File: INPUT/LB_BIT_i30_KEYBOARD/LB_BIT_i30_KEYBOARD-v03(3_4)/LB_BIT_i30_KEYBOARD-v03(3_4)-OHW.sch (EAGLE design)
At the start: 53 parts

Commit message: Updated licenses
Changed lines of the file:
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@@
 <?xml version="1.0" encoding="utf-8"?>
 <!DOCTYPE eagle SYSTEM "eagle.dtd">
-<eagle version="6.4">
+<eagle version="6.6.0">
 <drawing>
 <settings>
@@
 <layer number="225" name="225bmp" color="26" fill="10" visible="no" active="yes"/>
 <layer number="226" name="226bmp" color="27" fill="10" visible="no" active="yes"/>
+<layer number="227" name="227bmp" color="7" fill="1" visible="yes" active="yes"/>
+<layer number="228" name="228bmp" color="7" fill="1" visible="yes" active="yes"/>
 <layer number="248" name="Housing" color="7" fill="1" visible="yes" active="yes"/>
 <layer number="249" name="Edge" color="7" fill="1" visible="yes" active="yes"/>
@@
 <instance part="GND8" gate="1" x="43.18" y="5.08"/>
 <instance part="GND18" gate="1" x="187.96" y="78.74"/>
-<instance part="U$1" gate="G$1" x="236.22" y="50.8"/>
+<instance part="U$1" gate="G$1" x="20.32" y="12.7"/>
 <instance part="I30TVS3" gate="G$1" x="215.9" y="144.78" smashed="yes">
 <attribute name="NAME" x="212.8774" y="134.62" size="1.778" layer="95" rot="R90"/>
@@
 <instance part="GND19" gate="1" x="215.9" y="134.62"/>
 <instance part="GND20" gate="1" x="55.88" y="58.42"/>
-<instance part="U$2" gate="G$1" x="152.4" y="45.72"/>
+<instance part="U$2" gate="G$1" x="149.86" y="43.18"/>
 </instances>
 <busses>

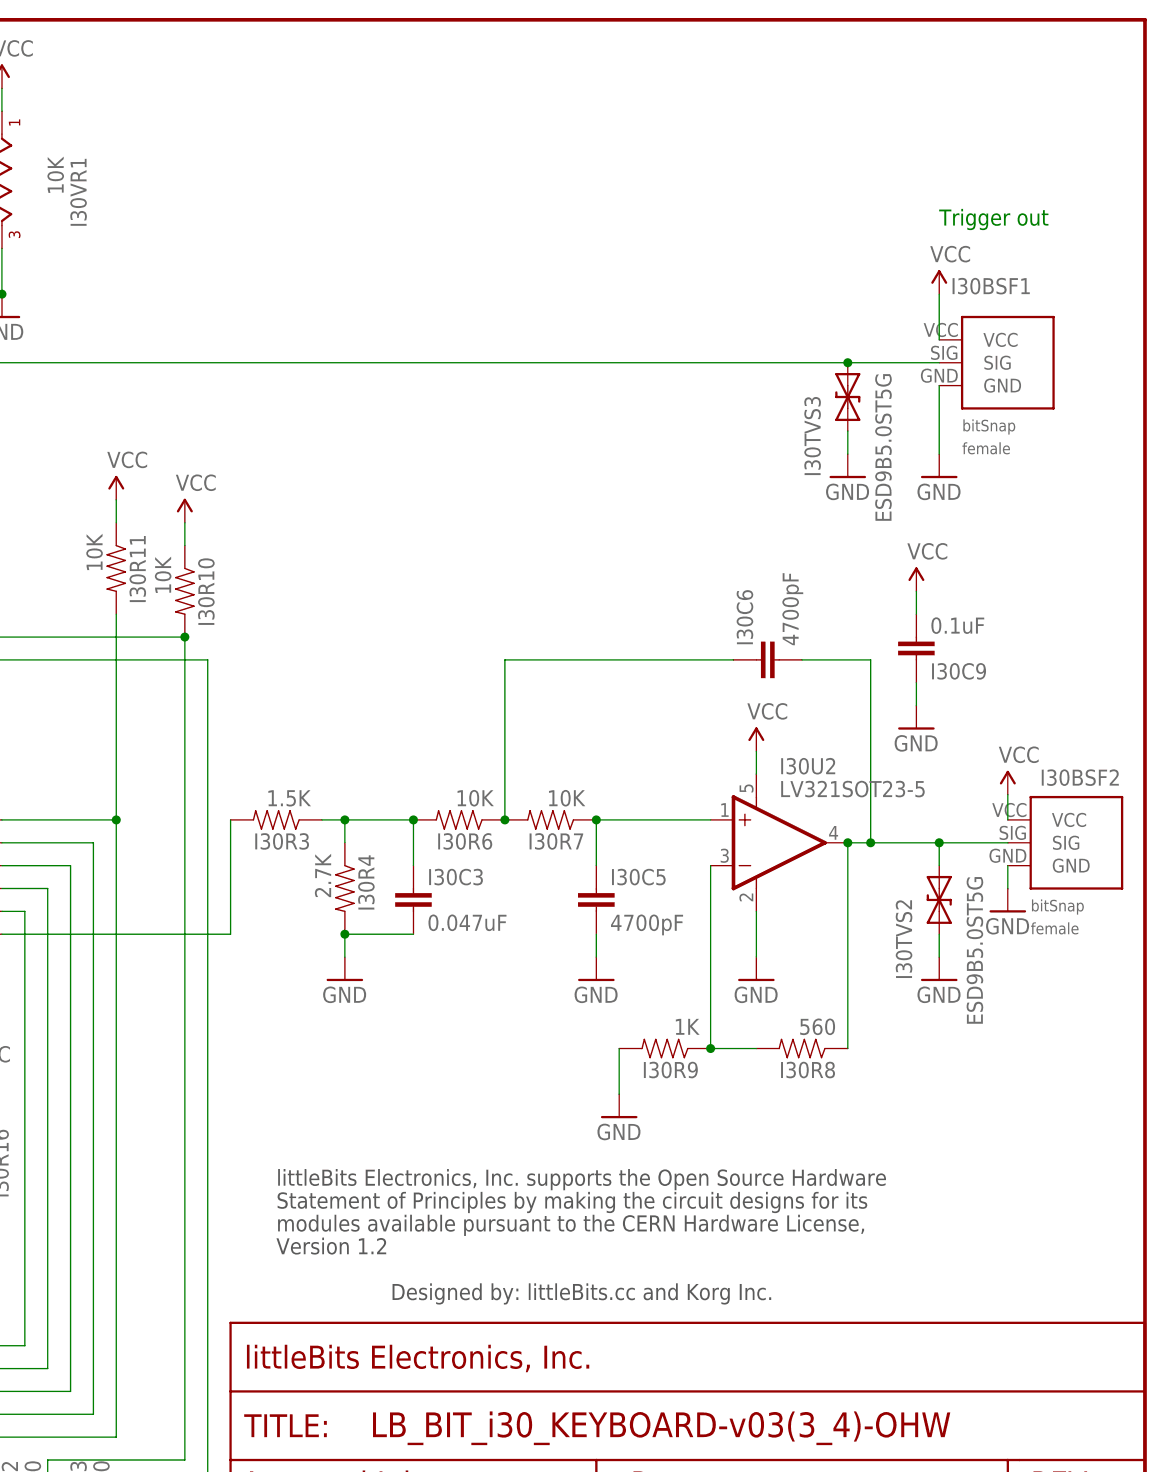
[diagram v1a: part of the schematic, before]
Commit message: Updated license in Korg bits modules
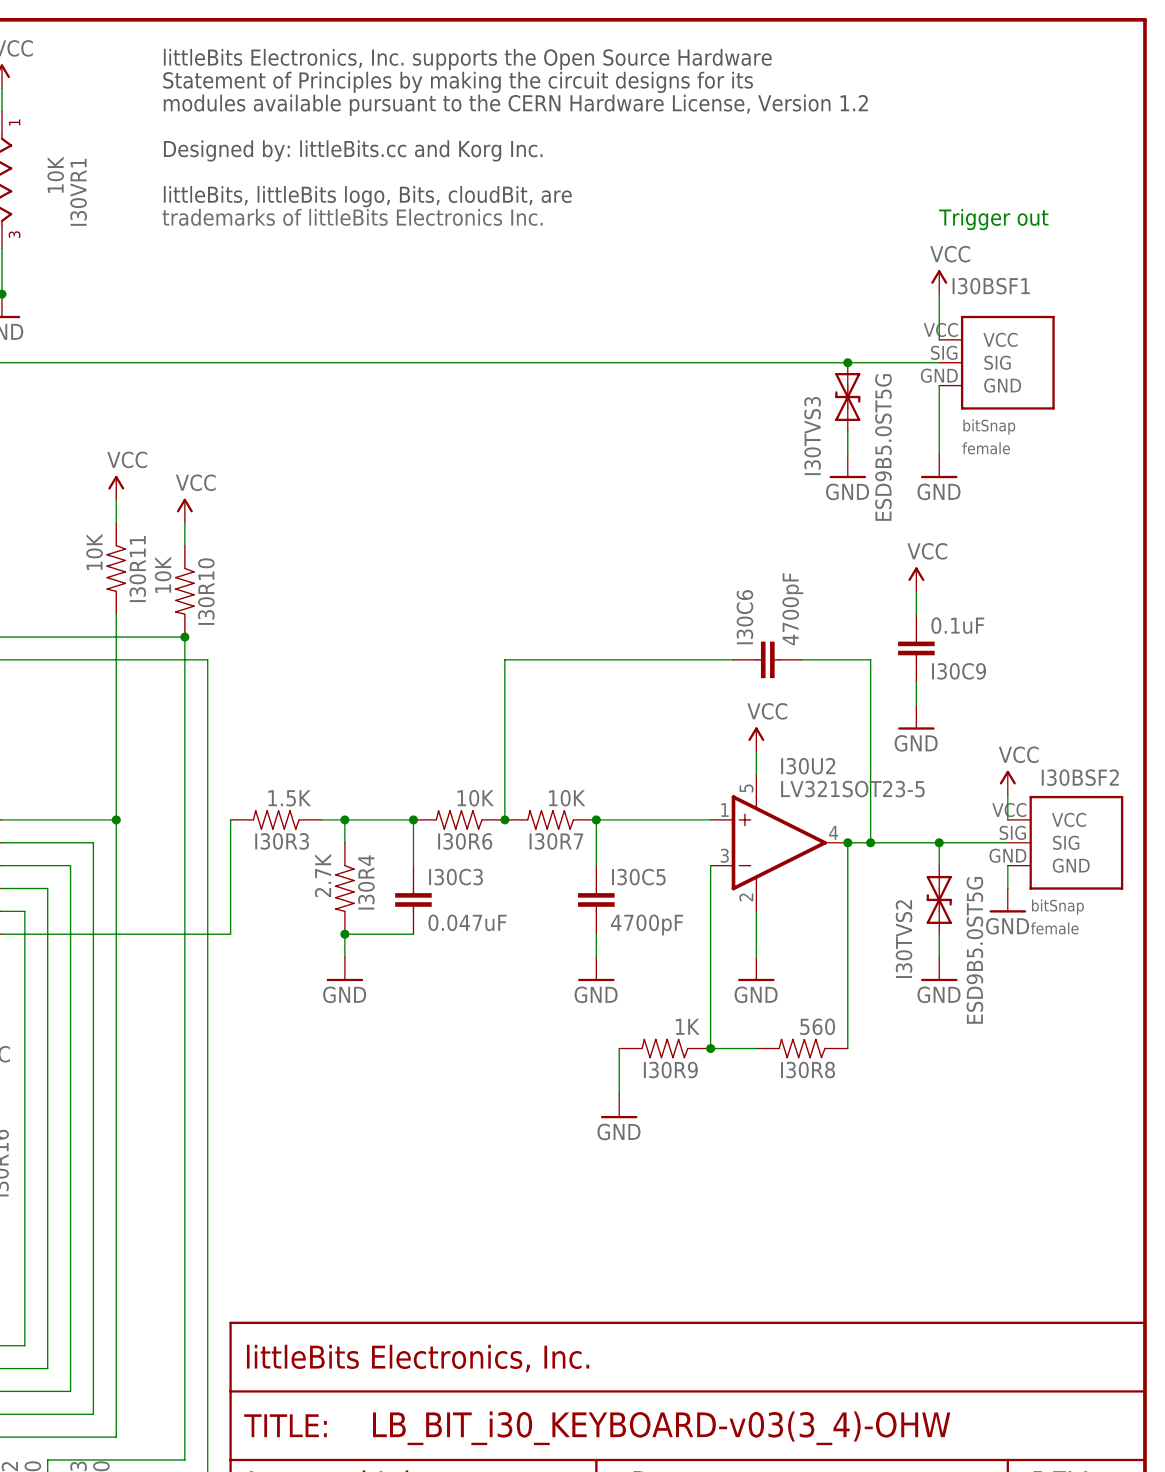
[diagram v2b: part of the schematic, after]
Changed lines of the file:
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@@
 <layer number="111" name="LB_TEXT" color="13" fill="1" visible="yes" active="yes"/>
 <layer number="112" name="tSilk" color="7" fill="1" visible="yes" active="yes"/>
+<layer number="113" name="ReferenceLS" color="7" fill="1" visible="yes" active="yes"/>
 <layer number="116" name="Patch_BOT" color="9" fill="4" visible="yes" active="yes"/>
+<layer number="118" name="Rect_Pads" color="7" fill="1" visible="yes" active="yes"/>
 <layer number="121" name="_tsilk" color="7" fill="1" visible="yes" active="yes"/>
 <layer number="122" name="_bsilk" color="7" fill="1" visible="yes" active="yes"/>
@@
 <instance part="GND19" gate="1" x="215.9" y="134.62"/>
 <instance part="GND20" gate="1" x="55.88" y="58.42"/>
-<instance part="U$2" gate="G$1" x="149.86" y="43.18"/>
+<instance part="U$2" gate="G$1" x="137.16" y="167.64"/>
 </instances>
 <busses>
